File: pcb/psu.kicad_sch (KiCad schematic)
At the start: 8 parts

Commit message: oops
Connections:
- net GND: now also C?.2
- net at R?.1: now also U?.6 (PG)
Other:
- moved on the sheet: C?
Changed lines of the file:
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@@
 (kicad_sch (version 20211123) (generator eeschema)
   (paper "A4")
+  (junction (at 171.45 59.69) (diameter 0) (color 0 0 0 0)
+  )
+  (junction (at 160.02 64.77) (diameter 0) (color 0 0 0 0)
+  )
+  (junction (at 224.155 90.17) (diameter 0) (color 0 0 0 0)
+  )
+  (junction (at 160.02 90.17) (diameter 0) (color 0 0 0 0)
+  )
+  (junction (at 224.155 49.53) (diameter 0) (color 0 0 0 0)
+  )
+  (junction (at 181.61 59.69) (diameter 0) (color 0 0 0 0)
+  )
   (junction (at 171.45 90.17) (diameter 0) (color 0 0 0 0)
   )
-  (junction (at 171.45 59.69) (diameter 0) (color 0 0 0 0)
-  )
-  (junction (at 160.02 64.77) (diameter 0) (color 0 0 0 0)
-  )
-  (junction (at 224.155 90.17) (diameter 0) (color 0 0 0 0)
-  )
-  (junction (at 160.02 90.17) (diameter 0) (color 0 0 0 0)
-  )
-  (junction (at 224.155 49.53) (diameter 0) (color 0 0 0 0)
-  )
   (junction (at 160.02 49.53) (diameter 0) (color 0 0 0 0)
   )
@@
   (junction (at 205.74 49.53) (diameter 0) (color 0 0 0 0)
   )
-  (wire (pts (xy 171.45 80.01) (xy 171.45 90.17))
-    (stroke (width 0) (type default) (color 0 0 0 0))
-  )
   (wire (pts (xy 160.02 49.53) (xy 205.74 49.53))
     (stroke (width 0) (type default) (color 0 0 0 0))
@@
     (stroke (width 0) (type default) (color 0 0 0 0))
   )
+  (wire (pts (xy 160.02 57.15) (xy 181.61 57.15))
+    (stroke (width 0) (type default) (color 0 0 0 0))
+  )
   (wire (pts (xy 232.41 49.53) (xy 232.41 58.42))
     (stroke (width 0) (type default) (color 0 0 0 0))
@@
     (stroke (width 0) (type default) (color 0 0 0 0))
   )
+  (wire (pts (xy 171.45 78.74) (xy 171.45 90.17))
+    (stroke (width 0) (type default) (color 0 0 0 0))
+  )
   (wire (pts (xy 181.61 59.69) (xy 181.61 107.95))
     (stroke (width 0) (type default) (color 0 0 0 0))
@@
     (stroke (width 0) (type default) (color 0 0 0 0))
   )
-  (wire (pts (xy 171.45 71.755) (xy 171.45 59.69))
-    (stroke (width 0) (type default) (color 0 0 0 0))
-  )
-  (wire (pts (xy 171.45 90.17) (xy 160.02 90.17))
+  (wire (pts (xy 160.02 90.17) (xy 171.45 90.17))
+    (stroke (width 0) (type default) (color 0 0 0 0))
+  )
+  (wire (pts (xy 181.61 57.15) (xy 181.61 59.69))
+    (stroke (width 0) (type default) (color 0 0 0 0))
+  )
+  (wire (pts (xy 171.45 71.12) (xy 171.45 59.69))
     (stroke (width 0) (type default) (color 0 0 0 0))
   )
@@
     (stroke (width 0) (type default) (color 0 0 0 0))
   )
+  (wire (pts (xy 160.02 90.17) (xy 137.16 90.17))
+    (stroke (width 0) (type default) (color 0 0 0 0))
+  )
+  (wire (pts (xy 171.45 59.69) (xy 173.99 59.69))
+    (stroke (width 0) (type default) (color 0 0 0 0))
+  )
+  (wire (pts (xy 160.02 54.61) (xy 198.12 54.61))
+    (stroke (width 0) (type default) (color 0 0 0 0))
+  )
+  (wire (pts (xy 137.16 76.2) (xy 137.16 90.17))
+    (stroke (width 0) (type default) (color 0 0 0 0))
+  )
   (wire (pts (xy 171.45 90.17) (xy 224.155 90.17))
-    (stroke (width 0) (type default) (color 0 0 0 0))
-  )
-  (wire (pts (xy 160.02 90.17) (xy 137.16 90.17))
-    (stroke (width 0) (type default) (color 0 0 0 0))
-  )
-  (wire (pts (xy 171.45 59.69) (xy 173.99 59.69))
-    (stroke (width 0) (type default) (color 0 0 0 0))
-  )
-  (wire (pts (xy 160.02 54.61) (xy 198.12 54.61))
-    (stroke (width 0) (type default) (color 0 0 0 0))
-  )
-  (wire (pts (xy 137.16 76.2) (xy 137.16 90.17))
     (stroke (width 0) (type default) (color 0 0 0 0))
   )
@@
     (pin "1")
   )
-  (symbol (lib_id "Device:C") (at 171.45 75.565 0) (unit 1)
-    (in_bom yes) (on_board yes) (fields_autoplaced)
-    (property "Reference" "C?" (id 0) (at 175.26 74.2949 0)
-      (effects (font (size 1.27 1.27)) (justify left))
-    )
-    (property "Value" "C" (id 1) (at 175.26 76.8349 0)
-      (effects (font (size 1.27 1.27)) (justify left))
-    )
-    (property "Footprint" "" (id 2) (at 172.4152 79.375 0)
-      (effects (font (size 1.27 1.27)) hide)
-    )
-    (property "Datasheet" "~" (id 3) (at 171.45 75.565 0)
-      (effects (font (size 1.27 1.27)) hide)
-    )
+  (symbol (lib_id "Device:C") (at 171.45 74.93 0) (unit 1)
+    (in_bom yes) (on_board yes) (fields_autoplaced)
+    (property "Reference" "C?" (id 0) (at 175.26 73.6599 0)
+      (effects (font (size 1.27 1.27)) (justify left))
+    )
+    (property "Value" "C" (id 1) (at 175.26 76.1999 0)
+      (effects (font (size 1.27 1.27)) (justify left))
+    )
+    (property "Footprint" "" (id 2) (at 172.4152 78.74 0)
+      (effects (font (size 1.27 1.27)) hide)
+    )
+    (property "Datasheet" "~" (id 3) (at 171.45 74.93 0)
+      (effects (font (size 1.27 1.27)) hide)
+    )

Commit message: more work on psu
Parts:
- added C? (x7): C, symbol Device:C
- added C?: C, symbol Device:C_Polarized
- added R? (x2): R, symbol Device:R
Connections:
- net +1V0: now also U?.1 (VO), R?.1
- net GND: now also U?.5 (GND), U?.EPAD, C?.2, C?.2, C?.2, C?.2, C?.2, C?.2, C?.2, C?.2, R?.2
- net at R?.1, U?.6 (PG): now also U?.5 (EN1)
- net POWER_IN: now reaches U?.1 (VIN1)
- net POWER_IN: now also U?.13 (VIN), U?.14 (VCC), U?.16 (VIN2), U?.7 (EN), C?.1, C?.1, C?.1, C?.1, C?.1, C?.1, C?.1
- net at U?.2 (VFB): now also R?.1, R?.2
- net at U?.4 (SS): now also C?.1
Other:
- moved on the sheet: C?, R?, U?

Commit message: finish wiring
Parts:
- added C? (x4): 22u, symbol Device:C
- added C? (x2): 100u, symbol Device:C
- added C?: C, symbol Device:C
- added FB?: FerriteBead, symbol Device:FerriteBead
- added L? (x2): INDUCTOR, symbol pspice:INDUCTOR
- added R? (x3): 22.1k, symbol Device:R
- added R?: 100k, symbol Device:R
- added R?: 73.2k, symbol Device:R
- added R?: 1, symbol Device:R
- C? (x3): value C -> 10u
- C?: value C -> 100u
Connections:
- net GND: now also U?.12 (EN2), U?.13 (PGND2), U?.4 (PGND1), U?.6 (PG1), U?.7 (VFB1), U?.8 (GND), C?.2, C?.2, C?.2, C?.2, C?.2, R?.1, R?.2, R?.2, R?.2, R?.2
- net at U?.10 (VFB2): now also R?.1, R?.2
- net at U?.14 (SW2): now also C?.2, L?.1
- net at U?.15 (VBST2): now also C?.1
- net at U?.2 (VBST1): now also C?.1
- net at U?.3 (SW1): now also C?.2, L?.2
- net at U?.9 (VREG5): now also C?.1, R?.1
- new net: FB?.2, R?.1
- new net +1V8: C?.1, C?.1, L?.1, R?.1
- new net +3.3V: C?.1, C?.1, FB?.1, L?.2, R?.1
- new net +3.3VA: R?.2
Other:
- moved on the sheet: C?, R?, U?

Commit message: finish psu(maybe???)
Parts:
- C? (x4): value 22u -> (none)
- C? (x3): value 100u -> (none)
- C?: value C -> 3.3n
- C?: value C -> (none)
- C? (x3): value 10u -> (none)
- C? (x2): value C -> 100n
- C? (x2): value C -> 22u
- C?: value C -> 100u
- C?: value C -> 1u
- C?: value C -> 10u
- FB?: value FerriteBead -> (none)
- L?: value INDUCTOR -> 1.5u
- L? (x2): value INDUCTOR -> (none)
- R? (x3): value 22.1k -> (none)
- R?: value 100k -> (none)
- R?: value R -> 6.8k
- R?: value R -> 22.1k
- R?: value 73.2k -> (none)
- R?: value R -> 100k
- R?: value 1 -> (none)
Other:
- note added: "1%"
- note added: "4.5V - 18V"
- moved on the sheet: C?, L?

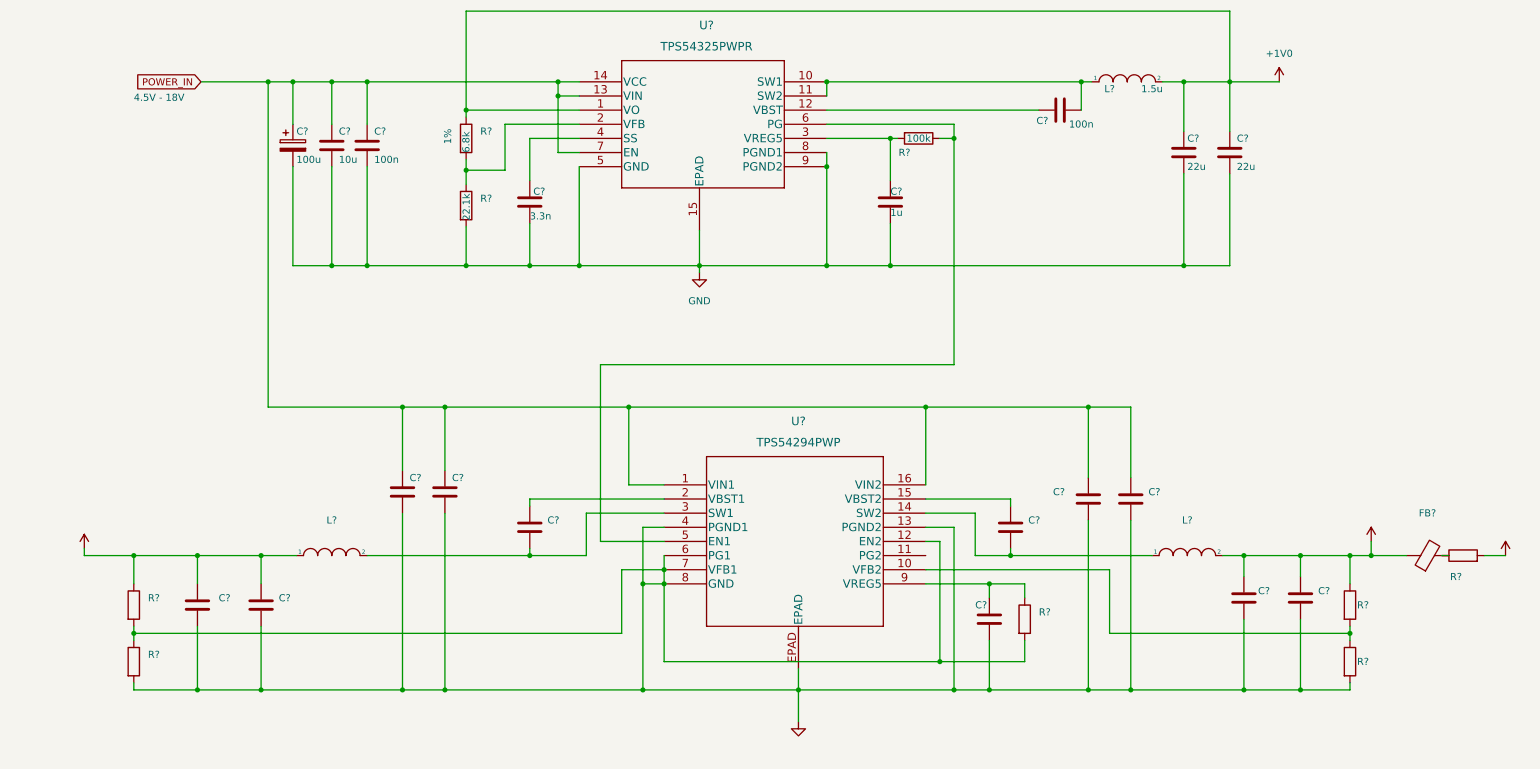
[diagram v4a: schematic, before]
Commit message: add component values
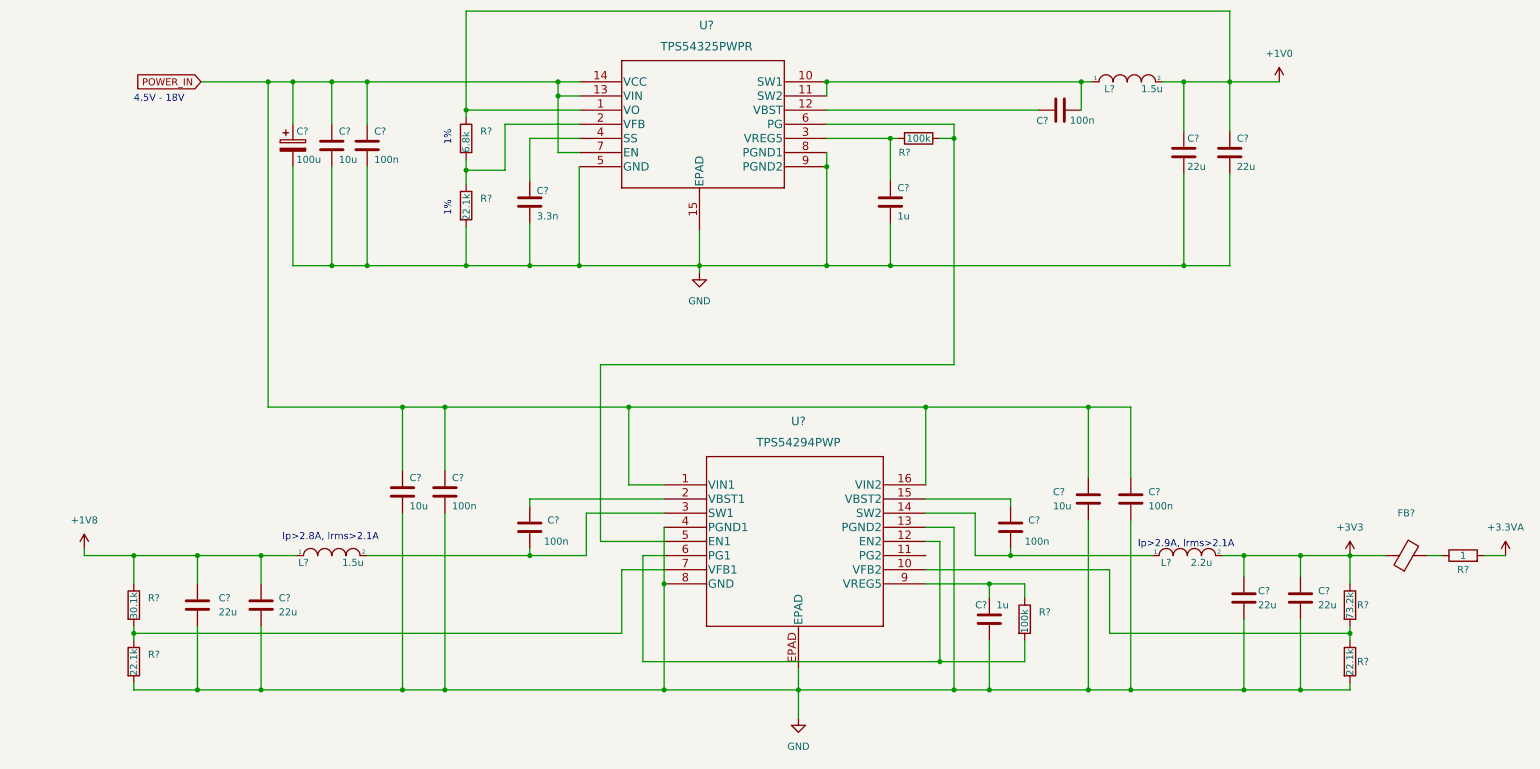
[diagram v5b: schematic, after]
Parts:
- C? (x4): value (none) -> 22u
- C? (x4): value (none) -> 100n
- C?: value (none) -> 1u
- C? (x2): value (none) -> 10u
- FB?: value (none) -> ~
- L?: value (none) -> 2.2u
- L?: value (none) -> 1.5u
- R?: value (none) -> 30.1k
- R?: value (none) -> 100k
- R? (x2): value (none) -> 22.1k
- R?: value (none) -> 73.2k
- R?: value (none) -> 1
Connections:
- net GND: no longer R?.1, R?.2, R?.2, U?.12 (EN2), U?.6 (PG1), U?.7 (VFB1)
- net +3.3V renamed +3V3
- new net: R?.1, R?.2, U?.7 (VFB1)
- new net: R?.2, U?.12 (EN2), U?.6 (PG1)
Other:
- note added: "lp>2.8A, lrms>2.1A"
- note added: "lp>2.9A, lrms>2.1A"
- moved on the sheet: FB?

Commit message: add jtag connector and flash to fpga
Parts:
- removed FB?: ~, symbol Device:FerriteBead
- removed R?: 1, symbol Device:R
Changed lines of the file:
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@@
-    (stroke (width 0) (type default) (color 0 0 0 0))
-  )
-  (wire (pts (xy 270.51 134.62) (xy 267.97 134.62))
     (stroke (width 0) (type default) (color 0 0 0 0))
   )
@@
     (stroke (width 0) (type default) (color 0 0 0 0))
   )
-  (wire (pts (xy 278.13 134.62) (xy 281.94 134.62))
-    (stroke (width 0) (type default) (color 0 0 0 0))
-  )
   (wire (pts (xy 95.25 54.61) (xy 95.25 36.83))
-    (stroke (width 0) (type default) (color 0 0 0 0))
-  )
-  (wire (pts (xy 254 134.62) (xy 260.35 134.62))
     (stroke (width 0) (type default) (color 0 0 0 0))
   )
@@
     (pin "2")
   )
-  (symbol (lib_id "power:+3.3VA") (at 281.94 134.62 0) (unit 1)
-    (in_bom yes) (on_board yes) (fields_autoplaced)
-    (property "Reference" "#PWR?" (id 0) (at 281.94 138.43 0)
-      (effects (font (size 1.27 1.27)) hide)
-    )
-    (property "Value" "+3.3VA" (id 1) (at 281.94 129.54 0))
-    (property "Footprint" "" (id 2) (at 281.94 134.62 0)
-      (effects (font (size 1.27 1.27)) hide)
-    )
-    (property "Datasheet" "" (id 3) (at 281.94 134.62 0)
-      (effects (font (size 1.27 1.27)) hide)
-    )
-    (pin "1")
-  )
   (symbol (lib_id "power:+1V8") (at 26.67 133.35 0) (unit 1)
     (in_bom yes) (on_board yes) (fields_autoplaced)
@@
     (pin "2")
   )
-  (symbol (lib_id "Device:FerriteBead") (at 264.16 134.62 90) (unit 1)
-    (in_bom yes) (on_board yes) (fields_autoplaced)
-    (property "Reference" "FB?" (id 0) (at 264.1092 127 90))
-    (property "Value" "~" (id 1) (at 264.1092 129.54 90))
-    (property "Footprint" "" (id 2) (at 264.16 136.398 90)
-      (effects (font (size 1.27 1.27)) hide)
-    )
-    (property "Datasheet" "~" (id 3) (at 264.16 134.62 0)
-      (effects (font (size 1.27 1.27)) hide)
-    )
-    (pin "1")
-    (pin "2")
-  )
   (symbol (lib_id "Device:C") (at 46.99 143.51 0) (unit 1)
     (in_bom yes) (on_board yes) (fields_autoplaced)
@@
       (effects (font (size 1.27 1.27)) hide)
     )
-    (pin "1")
-    (pin "2")
-  )
-  (symbol (lib_id "Device:R") (at 274.32 134.62 90) (unit 1)
-    (in_bom yes) (on_board yes)
-    (property "Reference" "R?" (id 0) (at 274.32 137.16 90))
-    (property "Value" "1" (id 1) (at 274.32 134.62 90))
-    (property "Footprint" "" (id 2) (at 274.32 136.398 90)
-      (effects (font (size 1.27 1.27)) hide)
-    )
-    (property "Datasheet" "~" (id 3) (at 274.32 134.62 0)
-      (effects (font (size 1.27 1.27)) hide)
-    )

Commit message: commit before merge
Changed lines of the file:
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@@
     (stroke (width 0) (type default) (color 0 0 0 0))
   )
-  (wire (pts (xy 232.41 49.53) (xy 241.3 49.53))
+  (wire (pts (xy 232.41 49.53) (xy 255.905 49.53))
     (stroke (width 0) (type default) (color 0 0 0 0))
   )
@@
     (effects (font (size 1.27 1.27)) (justify left bottom))
   )
-  (text "lp>2.9A, lrms>2.1A" (at 215.9 133.35 0)
+  (text "lp>2.9A, lrms>2.1A" (at 215.9 132.715 0)
     (effects (font (size 1.27 1.27)) (justify left bottom))
   )
@@
     (pin "2")
   )
-  (symbol (lib_id "power:+1V0") (at 241.3 49.53 0) (unit 1)
+  (symbol (lib_id "power:+1V0") (at 255.905 49.53 0) (unit 1)
     (in_bom yes) (on_board yes) (fields_autoplaced)
-    (property "Reference" "#PWR?" (id 0) (at 241.3 53.34 0)
-      (effects (font (size 1.27 1.27)) hide)
-    )
-    (property "Value" "+1V0" (id 1) (at 241.3 44.45 0))
-    (property "Footprint" "" (id 2) (at 241.3 49.53 0)
-      (effects (font (size 1.27 1.27)) hide)
-    )
-    (property "Datasheet" "" (id 3) (at 241.3 49.53 0)
-      (effects (font (size 1.27 1.27)) hide)
-    )
+    (property "Reference" "#PWR?" (id 0) (at 255.905 53.34 0)
+      (effects (font (size 1.27 1.27)) hide)
+    )
+    (property "Value" "+1V0" (id 1) (at 255.905 44.45 0))
+    (property "Footprint" "" (id 2) (at 255.905 49.53 0)
+      (effects (font (size 1.27 1.27)) hide)
+    )
+    (property "Datasheet" "" (id 3) (at 255.905 49.53 0)
+      (effects (font (size 1.27 1.27)) hide)
+    )
